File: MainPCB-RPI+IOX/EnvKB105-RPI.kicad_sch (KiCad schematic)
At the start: 247 parts, among them U1 Pico, U3 MCP23017_ML

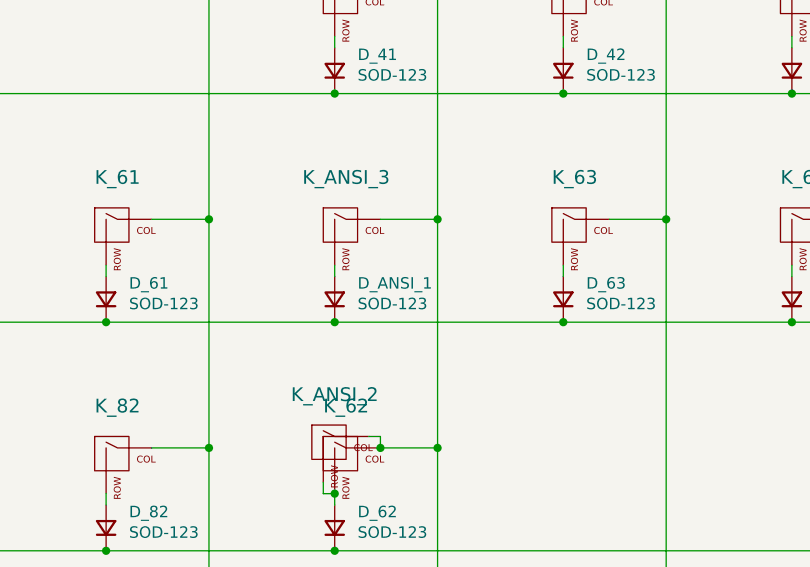
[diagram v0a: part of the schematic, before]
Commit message: fixed ref and generated updated gerber
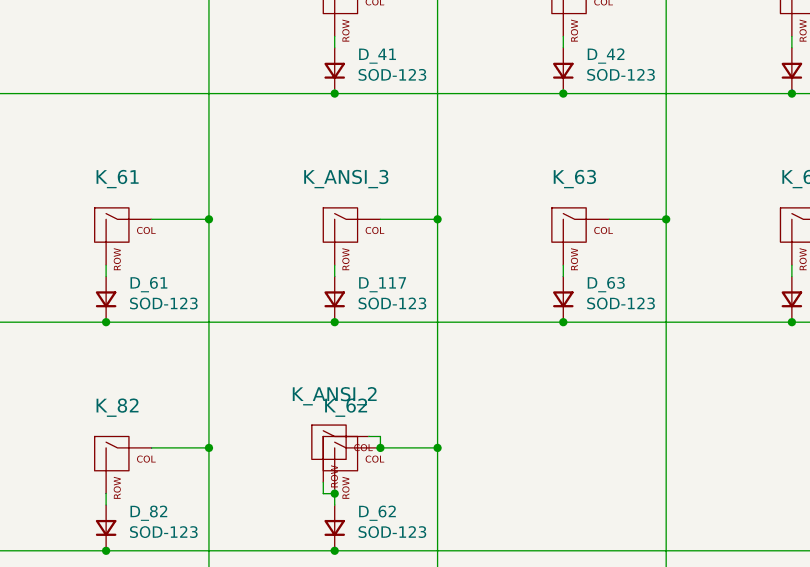
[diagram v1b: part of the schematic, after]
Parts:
- renumbered D_ANSI_1 to D_117
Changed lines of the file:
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@@
   (symbol (lib_id "Device:D_Small") (at 405.13 457.2 90) (unit 1)
     (in_bom yes) (on_board yes)
-    (property "Reference" "D_ANSI_1" (id 0) (at 407.67 455.422 90)
+    (property "Reference" "D_117" (id 0) (at 407.67 455.422 90)
       (effects (font (size 1.27 1.27)) (justify right))
     )
@@
     )
     (path "/00000000-0000-0000-0000-000061587a4c"
-      (reference "D_ANSI_1") (unit 1) (value "SOD-123") (footprint "Diode_SMD:D_SOD-123")
+      (reference "D_117") (unit 1) (value "SOD-123") (footprint "Diode_SMD:D_SOD-123")
     )
     (path "/00000000-0000-0000-0000-000060ccb1e5"

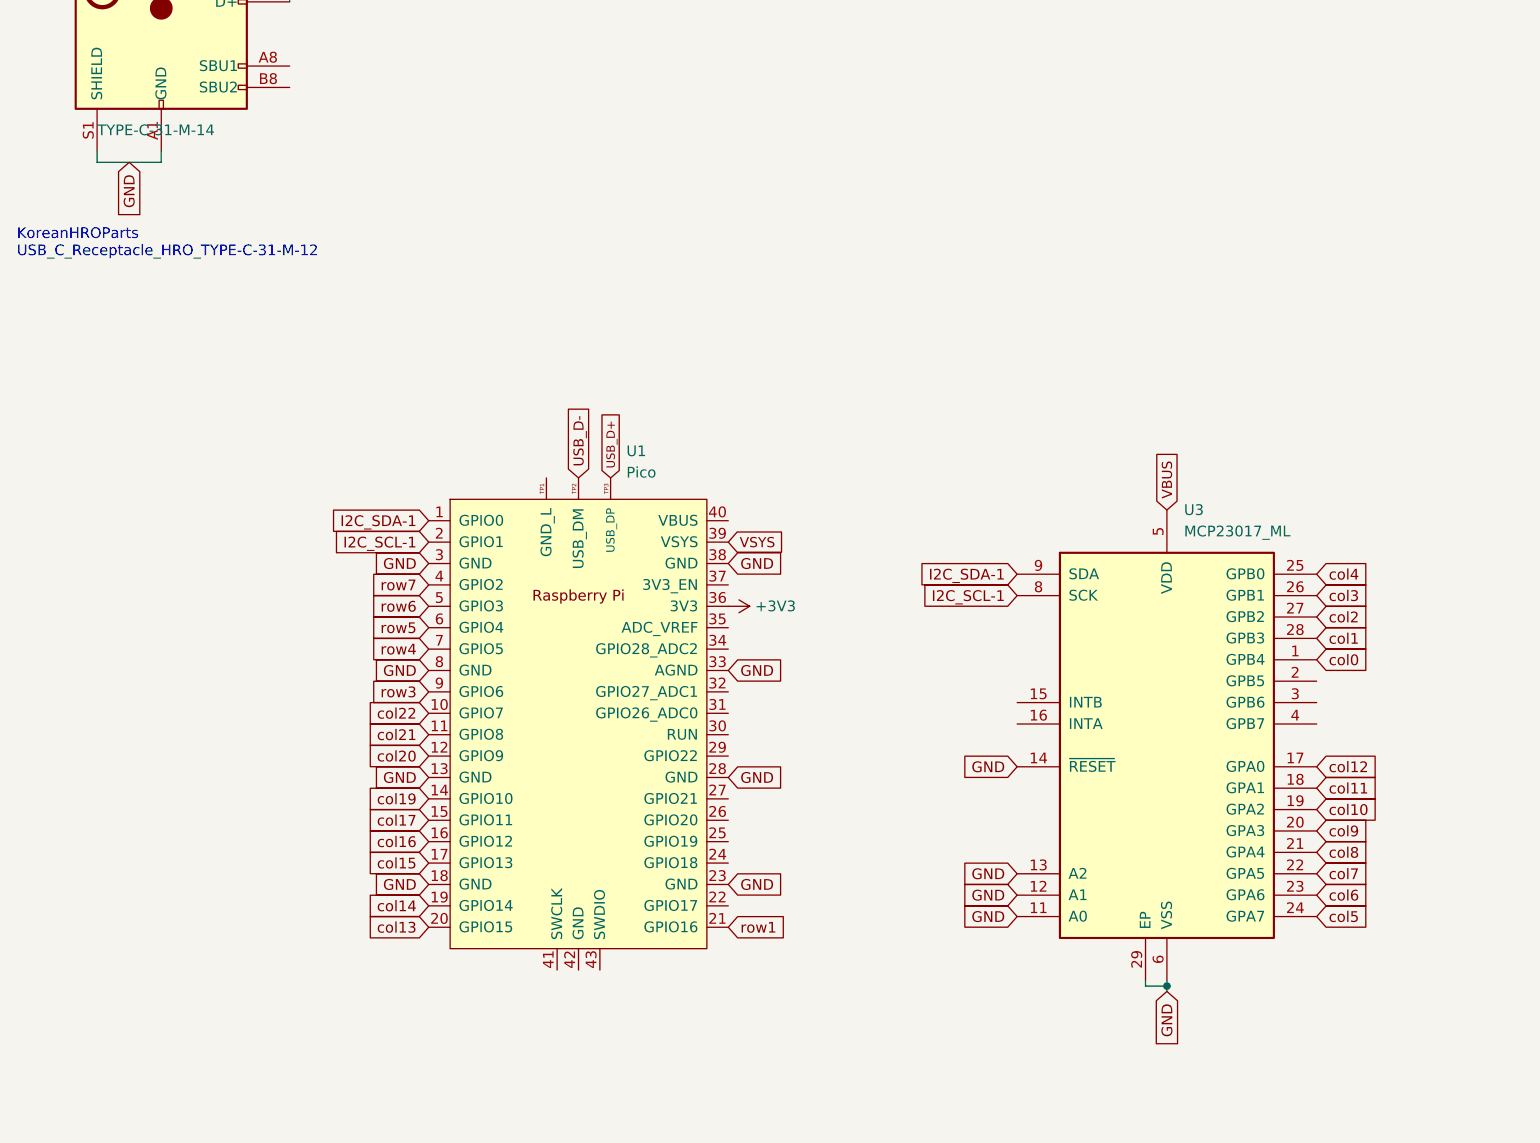
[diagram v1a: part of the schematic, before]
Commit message: swapped IO expander package to DIP
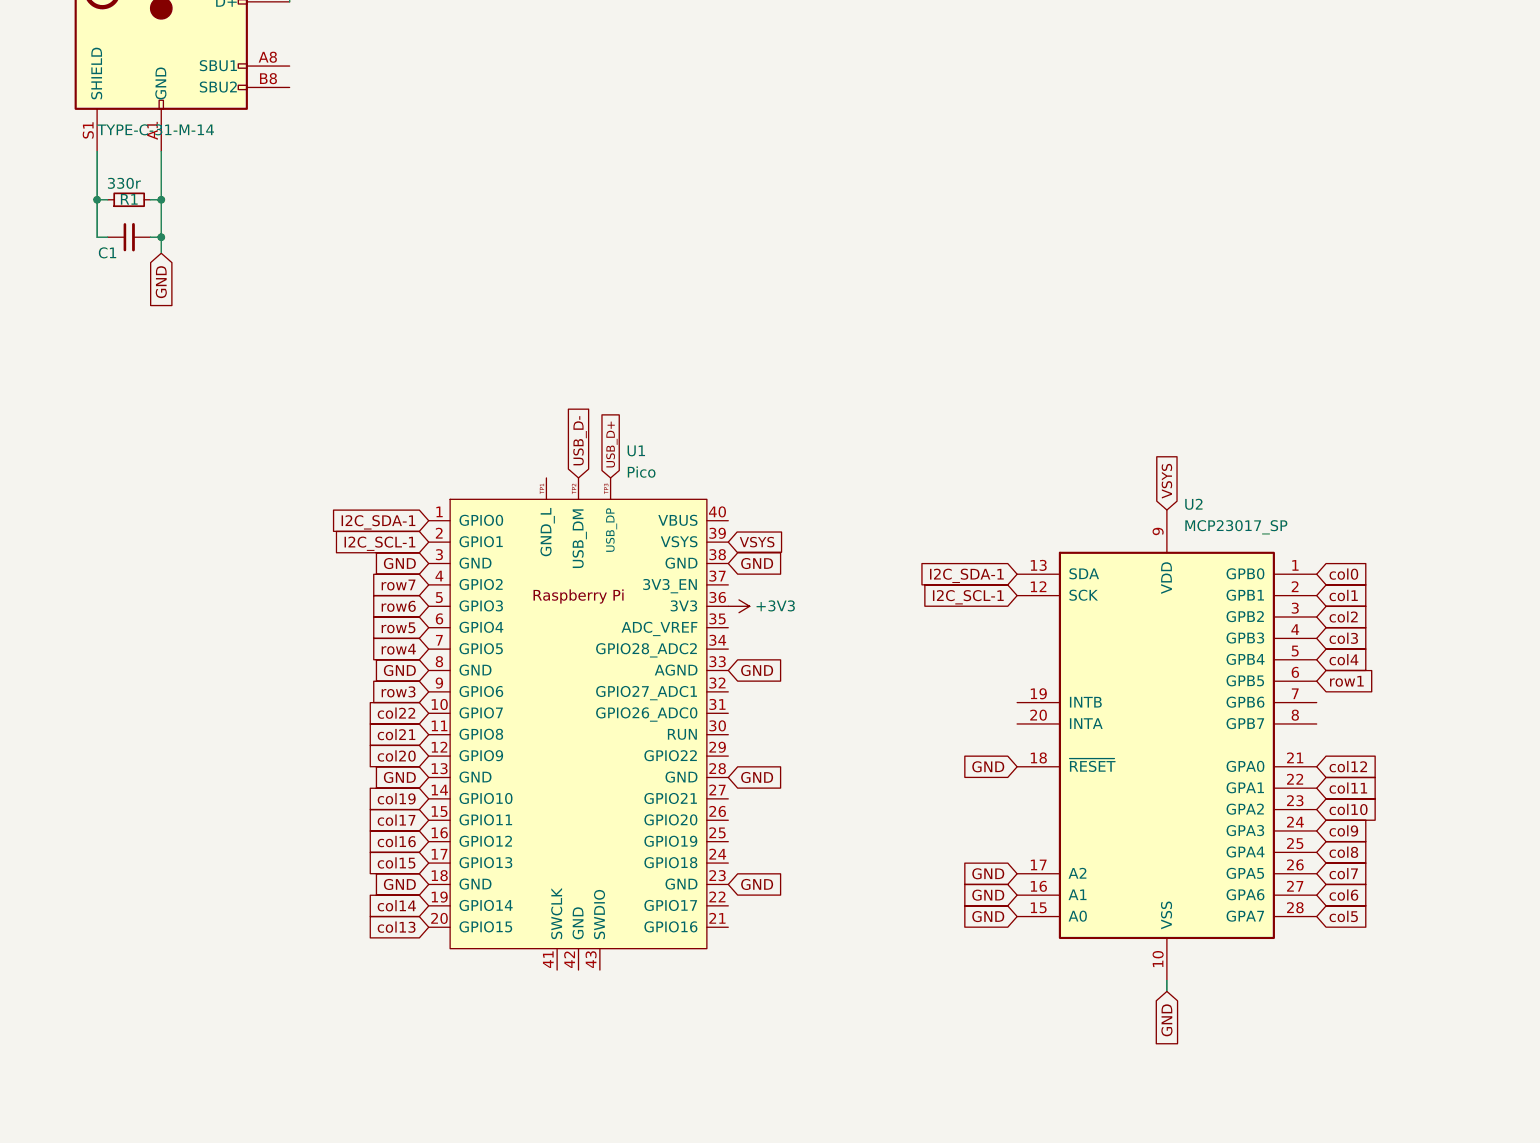
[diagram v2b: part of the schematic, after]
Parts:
- removed U3: MCP23017_ML, Package_DFN_QFN:QFN-28-1EP_6x6mm_P0.65mm_EP4.25x4.25mm, symbol Interface_Expansion:MCP23017_ML
- added C1: 0.1uf, Capacitor_SMD:C_0805_2012Metric, symbol Device:C_Small
- added R1: 330r, Resistor_SMD:R_0805_2012Metric, symbol Device:R_Small
- added U2: MCP23017_SP, Package_DIP:DIP-28_W7.62mm, symbol Interface_Expansion:MCP23017_SP
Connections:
- net GND: now also C1.2, R1.2, U2.10 (VSS), U2.15 (A0), U2.16 (A1), U2.17 (A2), U2.18 (~{RESET}); no longer USB1.S1 (SHIELD)
- net I2C_SCL-1: now also U2.12 (SCK)
- net I2C_SDA-1: now also U2.13 (SDA)
- net VSYS: now also U2.9 (VDD)
- net col0: now also U2.1 (GPB0)
- net col1: now also U2.2 (GPB1)
- net col10: now also U2.23 (GPA2)
- net col11: now also U2.22 (GPA1)
- net col12: now also U2.21 (GPA0)
- net col2: now also U2.3 (GPB2)
- net col3: now also U2.4 (GPB3)
- net col4: now also U2.5 (GPB4)
- net col5: now also U2.28 (GPA7)
- net col6: now also U2.27 (GPA6)
- net col7: now also U2.26 (GPA5)
- net col8: now also U2.25 (GPA4)
- net col9: now also U2.24 (GPA3)
- net row1: now also U2.6 (GPB5); no longer U1.21 (GPIO16)
- new net: C1.1, R1.1, USB1.S1 (SHIELD)
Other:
- note removed: "KoreanHROParts USB_C_Receptacle_HRO_TYPE-C-31-M-12"

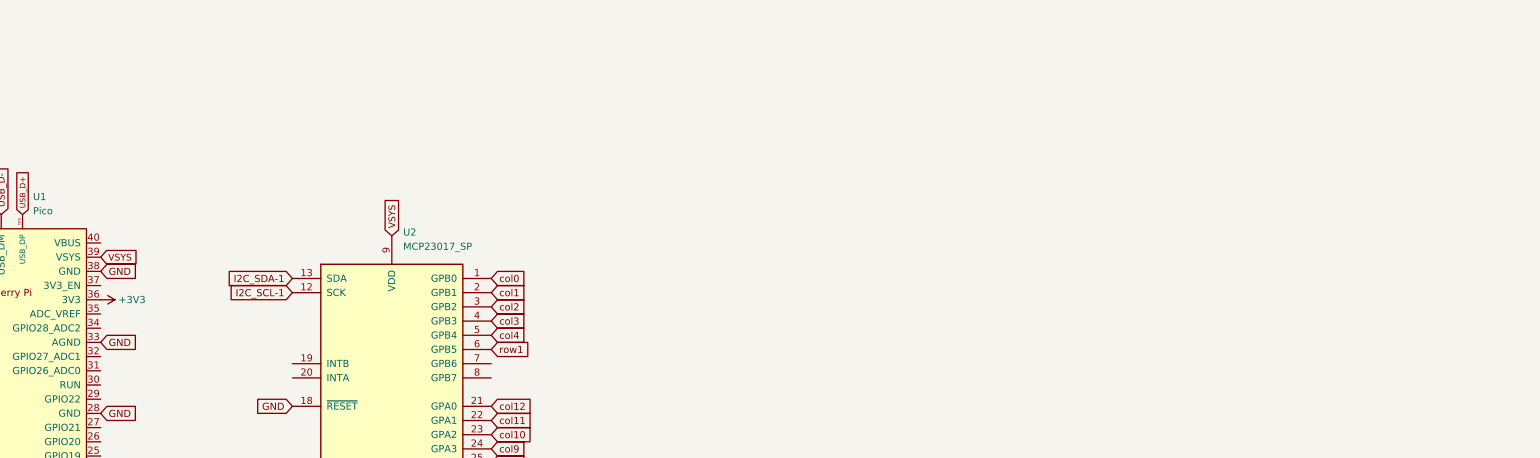
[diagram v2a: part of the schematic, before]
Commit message: Added position for OLED and RGB indicator LEDs among other things
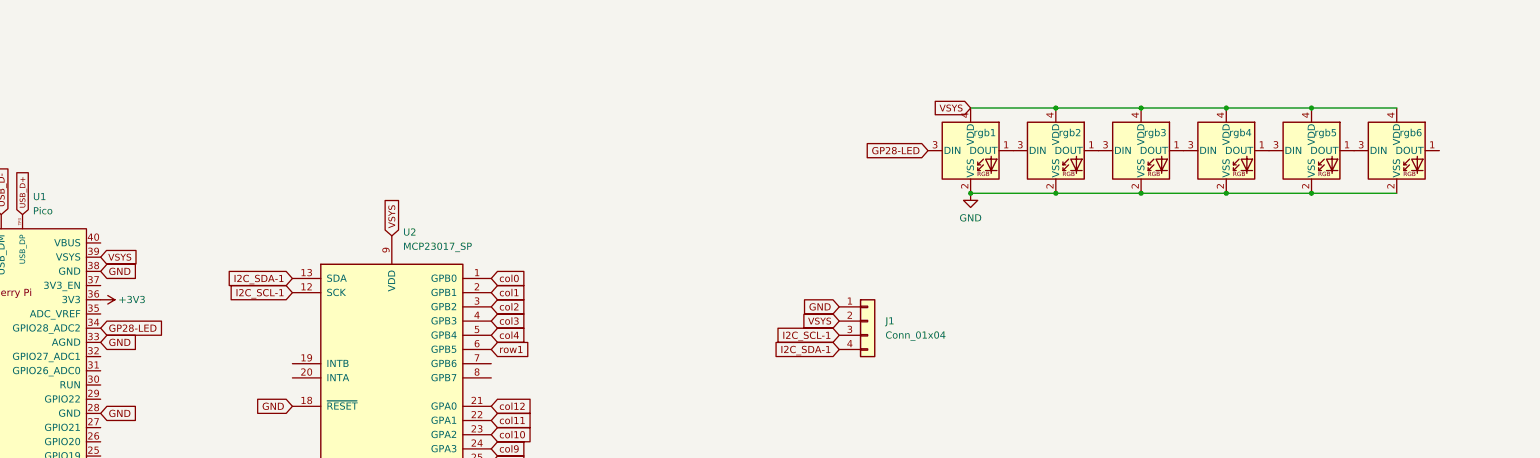
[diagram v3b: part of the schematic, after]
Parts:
- added J1: Conn_01x04, Connector_PinHeader_2.54mm:PinHeader_1x04_P2.54mm_Vertical, symbol Connector_Generic:Conn_01x04
- added rgb1, rgb2, rgb3, rgb4, rgb5, rgb6: SK6812MINI, LED_SMD:LED_SK6812MINI_PLCC4_3.5x3.5mm_P1.75mm, symbol LED:SK6812MINI
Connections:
- net GND: now also J1.1 (Pin_1), rgb1.2 (VSS), rgb2.2 (VSS), rgb3.2 (VSS), rgb4.2 (VSS), rgb5.2 (VSS), rgb6.2 (VSS)
- net I2C_SCL-1: now also J1.3 (Pin_3)
- net I2C_SDA-1: now also J1.4 (Pin_4)
- net VSYS: now also J1.2 (Pin_2), rgb1.4 (VDD), rgb2.4 (VDD), rgb3.4 (VDD), rgb4.4 (VDD), rgb5.4 (VDD), rgb6.4 (VDD)
- net GP28-LED: now reaches U1.34 (GPIO28_ADC2)
- net GP28-LED: now also rgb1.3 (DIN)
- new net: rgb4.1 (DOUT), rgb5.3 (DIN)
- new net: rgb3.1 (DOUT), rgb4.3 (DIN)
- new net: rgb2.1 (DOUT), rgb3.3 (DIN)
- new net: rgb1.1 (DOUT), rgb2.3 (DIN)
- new net: rgb5.1 (DOUT), rgb6.3 (DIN)

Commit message: some adjustments to make CAD a bit easier
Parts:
- H1, H10, H11, H12, H13, H14, H15, H16, H17, H18, H2, H3, H4, H5, H6, H7, H8, H9: footprint MountingHole:MountingHole_2.2mm_M2_Pad -> EnvExtras:MountingHole_2.2mm_M2_Pad-Mod

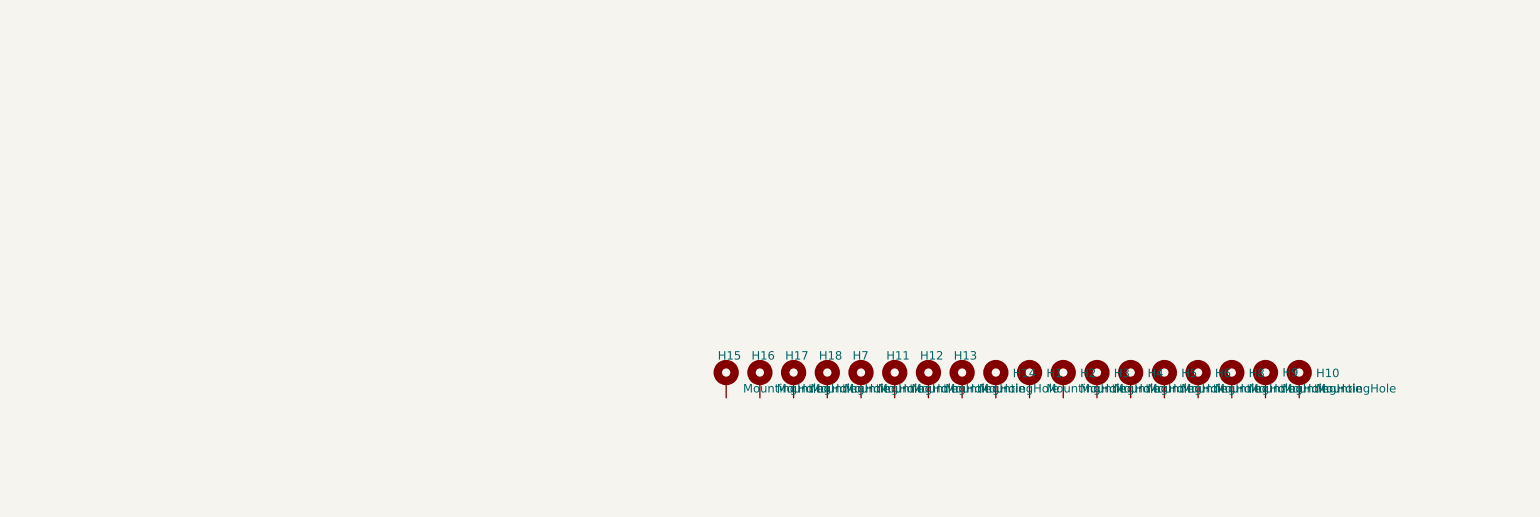
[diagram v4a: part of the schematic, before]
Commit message: Changed my mind on Mount holes
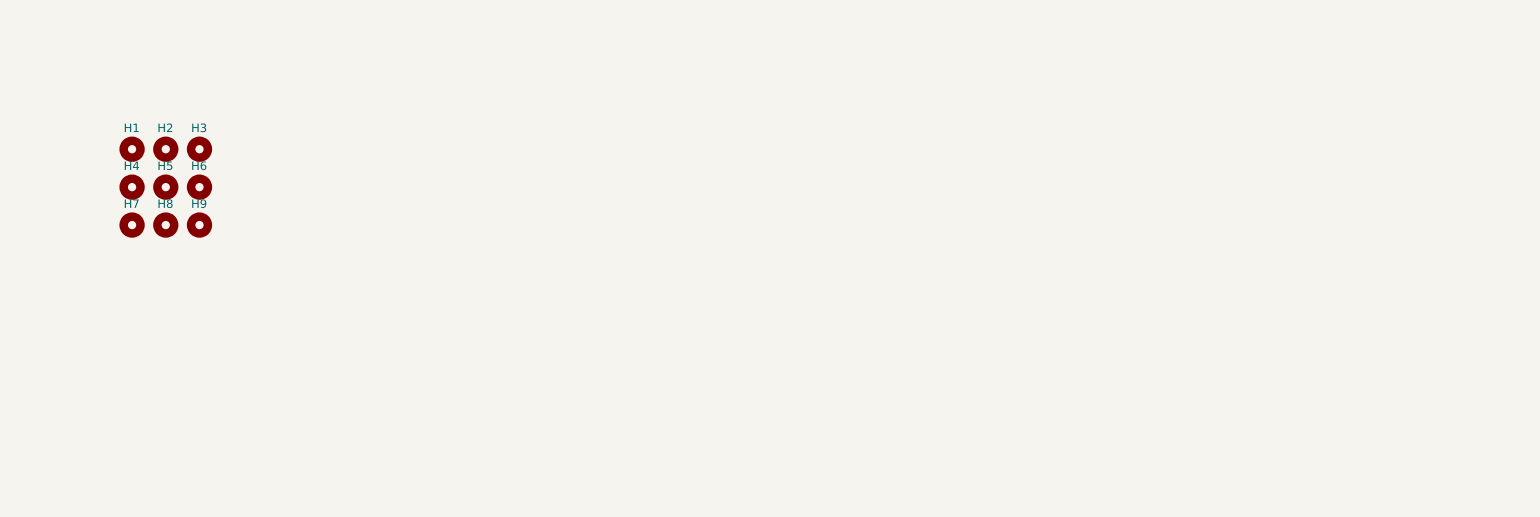
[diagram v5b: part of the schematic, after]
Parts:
- removed H1, H10, H11, H12, H13, H14, H15, H16, H17, H18, H2, H3, H4, H5, H6, H7, H8, H9: MountingHole, EnvExtras:MountingHole_2.2mm_M2_Pad-Mod, symbol Mechanical:MountingHole_Pad
- added H1, H2, H3, H4, H5, H6, H7, H8, H9: MountingHole, EnvExtras:MountingHole_2.2mm_M2_Pad-Mod, symbol Mechanical:MountingHole

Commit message: added 7u bottom and stepped capslock
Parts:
- added K_104B1, K_105B1, K_106B1, K_107B1, K_108B1, K_109B1, K_111B1, K_70B1: KEYSW, EnvExtras:MXOnly-1U-Hotswap-Modified, symbol MX_Alps_Hybrid:MX-NoLED
- added stab101: MountingHole, Mounting_Keyboard_Stabilizer:Stabilizer_Cherry_MX_7u, symbol Mechanical:MountingHole
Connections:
- net col0: now also K_104B1.1 (COL), K_70B1.1 (COL)
- net col1: now also K_105B1.1 (COL)
- net col11: now also K_108B1.1 (COL)
- net col13: now also K_109B1.1 (COL)
- net col14: now also K_111B1.1 (COL)
- net col3: now also K_106B1.1 (COL)
- net col6: now also K_107B1.1 (COL)
- net at D_70.2 (A), K_70.2 (ROW): now also K_70B1.2 (ROW)
- net at D_104.2 (A), K_104.2 (ROW): now also K_104B1.2 (ROW)
- net at D_105.2 (A), K_105.2 (ROW): now also K_105B1.2 (ROW)
- net at D_106.2 (A), K_106.2 (ROW): now also K_106B1.2 (ROW)
- net at D_107.2 (A), K_107.2 (ROW): now also K_107B1.2 (ROW)
- net at D_109.2 (A), K_109.2 (ROW): now also K_108B1.2 (ROW)
- net at D_110.2 (A), K_110.2 (ROW): now also K_109B1.2 (ROW)
- net at D_111.2 (A), K_111.2 (ROW): now also K_111B1.2 (ROW)

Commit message: various small adjustments
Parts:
- R5, R6: footprint Resistor_SMD:R_0402_1005Metric -> Resistor_SMD:R_0805_2012Metric
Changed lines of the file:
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@@
       (effects (font (size 0.508 0.508)))
     )
-    (property "Footprint" "Resistor_SMD:R_0402_1005Metric" (id 2) (at 48.895 33.02 0)
+    (property "Footprint" "Resistor_SMD:R_0805_2012Metric" (id 2) (at 48.895 33.02 0)
       (effects (font (size 1.27 1.27)) hide)
     )
@@
       (effects (font (size 0.508 0.508)))
     )
-    (property "Footprint" "Resistor_SMD:R_0402_1005Metric" (id 2) (at 48.895 30.48 0)
+    (property "Footprint" "Resistor_SMD:R_0805_2012Metric" (id 2) (at 48.895 30.48 0)
       (effects (font (size 1.27 1.27)) hide)
     )
@@
     )
     (path "/00000000-0000-0000-0000-00006093a5b0"
-      (reference "R5") (unit 1) (value "5.1K 0402") (footprint "Resistor_SMD:R_0402_1005Metric")
+      (reference "R5") (unit 1) (value "5.1K 0402") (footprint "Resistor_SMD:R_0805_2012Metric")
     )
     (path "/00000000-0000-0000-0000-0000609385d4"
-      (reference "R6") (unit 1) (value "5.1K 0402") (footprint "Resistor_SMD:R_0402_1005Metric")
+      (reference "R6") (unit 1) (value "5.1K 0402") (footprint "Resistor_SMD:R_0805_2012Metric")
     )
     (path "/c8babb31-7ea1-4408-b1ff-2852f4b242b1"
